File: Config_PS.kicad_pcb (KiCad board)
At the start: 2 copper layers, 46.3 x 25.2 mm, 13 parts, among them J1 Barrel_Jack_Switch, J2 Conn_01x03_Pin, J3 Screw_Terminal_01x02, U1 LM317_TO-220, U2 LM7805_TO220

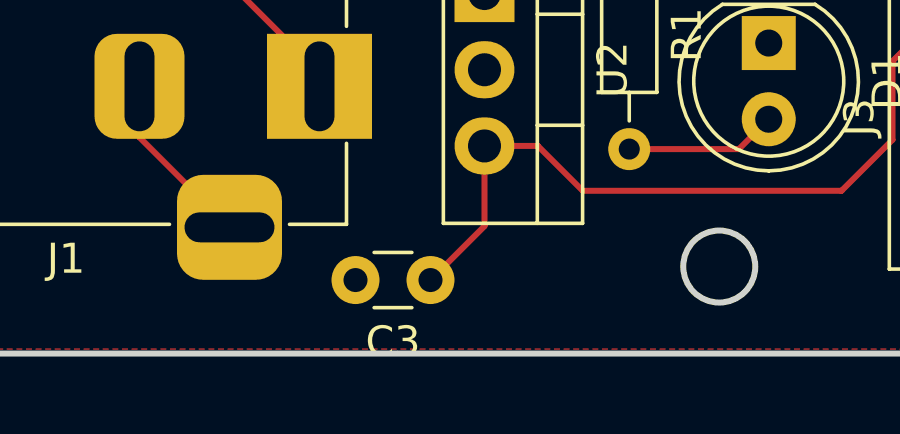
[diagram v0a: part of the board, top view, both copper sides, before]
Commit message: added custom logo
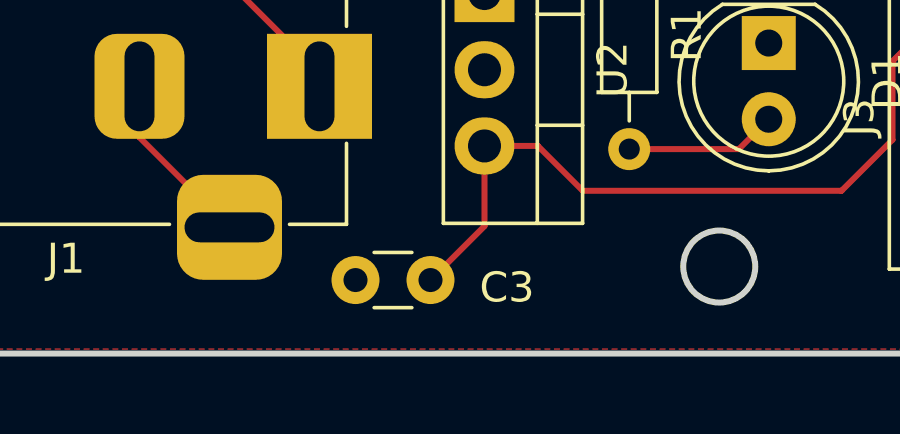
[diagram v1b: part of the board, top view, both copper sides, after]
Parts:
- added G***: LOGO, logo_Footprints:coretech_logo, B.Cu at (212.3, 86.0)
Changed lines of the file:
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@@
 		(tags "C Disc series Radial pin pitch 2.50mm  diameter 3.0mm width 1.6mm Capacitor")
 		(property "Reference" "C3"
-			(at 1.25 -2.05 0)
+			(at -2.55 -0.25 0)
 			(layer "F.SilkS")
 			(effects
@@
 		)
 	)
+	(footprint "logo_Footprints:coretech_logo"
+		(layer "B.Cu")
+		(at 212.3 86.025)
+		(property "Reference" "G***"
+			(at 0 0 0)
+			(layer "B.SilkS")
+			(hide yes)
+			(effects
+				(font
+					(size 1.5 1.5)
+					(thickness 0.3)
+				)
+				(justify mirror)
+			)
+		)
+		(property "Value" "LOGO"
+			(at 0.75 0 0)
+			(layer "B.SilkS")
+			(hide yes)
+			(effects
+				(font
+					(size 1.5 1.5)
+					(thickness 0.3)
+				)
+				(justify mirror)
+			)
+		)
+		(property "Footprint" "logo_Footprints:coretech_logo"
+			(at 0 0 0)
+			(layer "B.Fab")
+			(hide yes)
+			(effects
+				(font
+					(size 1.27 1.27)
+					(thickness 0.15)
+				)
+				(justify mirror)
+			)
+		)
+		(property "Datasheet" ""
+			(at 0 0 0)
+			(layer "B.Fab")
+			(hide yes)
+			(effects
+				(font
+					(size 1.27 1.27)
+					(thickness 0.15)
+				)
+				(justify mirror)
+			)
+		)
+		(property "Description" ""
+			(at 0 0 0)
+			(layer "B.Fab")
+			(hide yes)
+			(effects
+				(font
+					(size 1.27 1.27)
+					(thickness 0.15)
+				)
+				(justify mirror)
+			)
+		)
+		(attr board_only exclude_from_pos_files exclude_from_bom)
+		(fp_poly
+			(pts
+				(xy 5.054071 3.599656) (xy 4.485457 2.615288) (xy 4.238455 3.054834) (xy 4.102862 3.294508) (xy 3.991063 3.489236)
+				(xy 3.930786 3.591044) (xy 3.871041 3.627731) (xy 3.733976 3.652791) (xy 3.502225 3.667191) (xy 3.158418 3.671896)
+				(xy 2.685187 3.667871) (xy 2.578788 3.666192) (xy 1.287457 3.644675) (xy 2.259569 2.046331) (xy 3.231682 0.447987)
+				(xy 2.883213 -0.151746) (xy 2.726388 -0.413236) (xy 2.595394 -0.616116) (xy 2.509253 -0.731664)
+				(xy 2.488527 -0.747702) (xy 2.439953 -0.684959) (xy 2.322781 -0.508357) (xy 2.146269 -0.232597)
+				(xy 1.919676 0.127621) (xy 1.652259 0.557598) (xy 1.353278 1.042635) (xy 1.09226 1.469162) (xy -0.257788 3.682249)
+				(xy -2.643549 3.682249) (xy -5.029311 3.682249) (xy -5.335503 4.133137) (xy -5.641694 4.584024)
+				(xy -0.009505 4.584024) (xy 5.622685 4.584024)
+			)
+			(stroke
+				(width 0)
+				(type solid)
+			)
+			(fill solid)
+			(layer "B.SilkS")
+		)
+		(fp_poly
+			(pts
+				(xy -2.630952 3.28887) (xy -0.436237 3.268935) (xy 0.153121 2.273225) (xy 0.74248 1.277515) (xy 0.028361 1.277515)
+				(xy -0.685757 1.277515) (xy -0.907236 1.765977) (xy -1.128715 2.254438) (xy -1.960723 2.254438)
+				(xy -2.792731 2.254438) (xy -2.644872 2.010208) (xy -2.570816 1.88623) (xy -2.431011 1.650623) (xy -2.236017 1.321238)
+				(xy -1.996391 0.915929) (xy -1.722692 0.45255) (xy -1.425479 -0.051045) (xy -1.278286 -0.300591)
+				(xy -0.981021 -0.804296) (xy -0.708775 -1.264917) (xy -0.470771 -1.666903) (xy -0.276234 -1.994699)
+				(xy -0.134388 -2.232753) (xy -0.054458 -2.365514) (xy -0.040197 -2.388053) (xy 0.01069 -2.34216)
+				(xy 0.130975 -2.201719) (xy 0.299409 -1.992065) (xy 0.396656 -1.86711) (xy 0.814147 -1.325273) (xy 0.389078 -0.493554)
+				(xy 0.224535 -0.171153) (xy 0.085285 0.102523) (xy -0.014586 0.299731) (xy -0.06099 0.392727) (xy -0.061831 0.394527)
+				(xy -0.004668 0.41989) (xy 0.170106 0.439332) (xy 0.429834 0.449851) (xy 0.551293 0.450888) (xy 1.190258 0.450888)
+				(xy 1.697299 -0.356823) (xy 1.88939 -0.668566) (xy 2.04809 -0.937058) (xy 2.158038 -1.135506) (xy 2.203872 -1.237118)
+				(xy 2.20434 -1.241166) (xy 2.167668 -1.325763) (xy 2.065524 -1.516878) (xy 1.909712 -1.794613) (xy 1.712037 -2.139074)
+				(xy 1.484302 -2.530365) (xy 1.238314 -2.94859) (xy 0.985876 -3.373855) (xy 0.738794 -3.786262) (xy 0.508872 -4.165918)
+				(xy 0.307915 -4.492926) (xy 0.147727 -4.747391) (xy 0.040113 -4.909418) (xy -0.002033 -4.959763)
+				(xy -0.047709 -4.896469) (xy -0.161533 -4.71412) (xy -0.336842 -4.424011) (xy -0.566972 -4.037438)
+				(xy -0.845257 -3.565699) (xy -1.165034 -3.020089) (xy -1.519638 -2.411905) (xy -1.902403 -1.752443)
+				(xy -2.296366 -1.070858) (xy -2.704239 -0.363829) (xy -3.092974 0.309943) (xy -3.455503 0.938217)
+				(xy -3.784759 1.508748) (xy -4.073676 2.009293) (xy -4.315186 2.427607) (xy -4.502222 2.751448)
+				(xy -4.627717 2.968571) (xy -4.682675 3.063427) (xy -4.825667 3.308805)
+			)
+			(stroke
+				(width 0)
+				(type solid)
+			)
+			(fill solid)
+			(layer "B.SilkS")
+		)
+	)
